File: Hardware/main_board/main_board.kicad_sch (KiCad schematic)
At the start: 115 parts, among them J1 ALARM, J2 RFID_CONN, J3 GPS_CONN, J4 USB_A, J5 DEBUG, J6 ANTENNA2, J7 Conn_01x04_Male, J8 BATT, SW1 SW_Push, SW2 SW_Push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

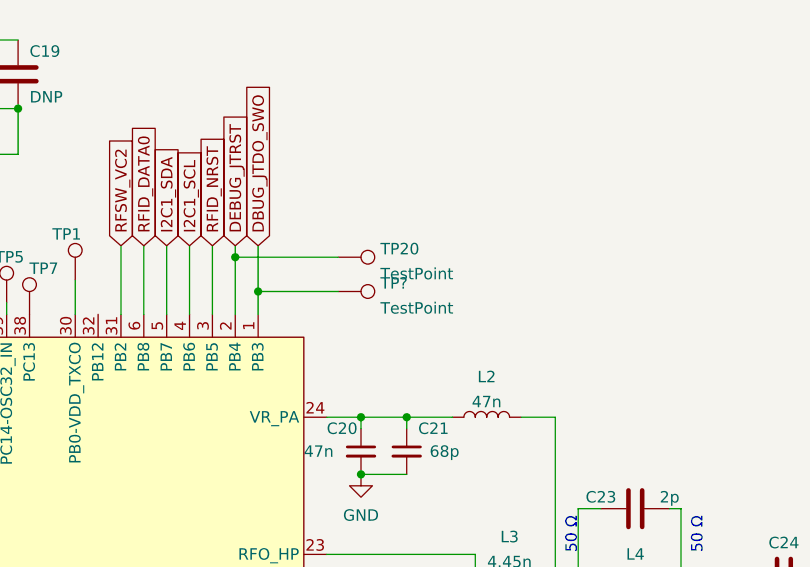
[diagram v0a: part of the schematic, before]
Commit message: all boards pass DRC and have appropriate silkscreens, will order tomorrow
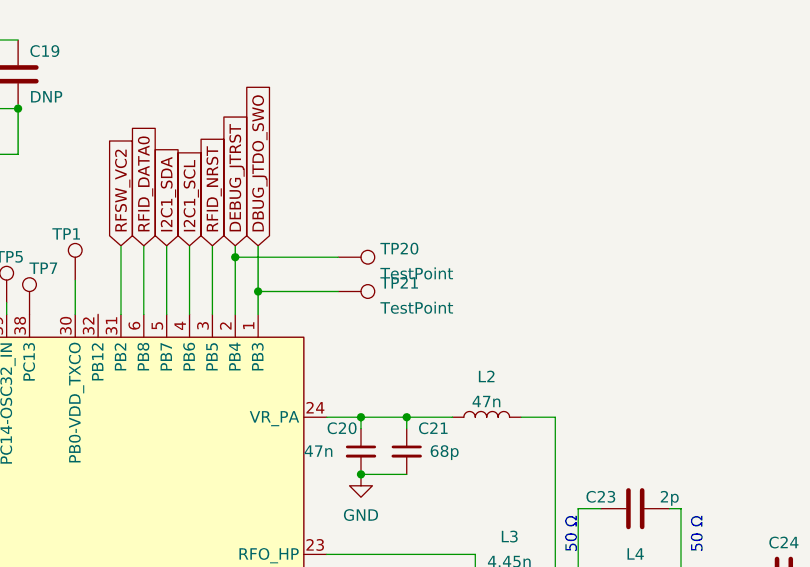
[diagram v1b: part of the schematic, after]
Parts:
- D5, D6, D7, D8: footprint LED_SMD:LED_0805_2012Metric -> LED_SMD:LED_0603_1608Metric
- H1, H2, H3, H4: footprint MountingHole:MountingHole_3.2mm_M3_Pad_Via -> MountingHole:MountingHole_2.2mm_M2_Pad_Via
- R15: footprint Resistor_SMD:R_0805_2012Metric_Pad1.20x1.40mm_HandSolder -> Resistor_SMD:R_0603_1608Metric
- TP21: renamed from TP?; footprint (none) -> TestPoint:TestPoint_Pad_1.0x1.0mm
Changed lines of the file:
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@@
       (effects (font (size 1.27 1.27)) (justify right))
     )
-    (property "Footprint" "LED_SMD:LED_0805_2012Metric" (id 2) (at 387.35 46.99 0)
+    (property "Footprint" "LED_SMD:LED_0603_1608Metric" (id 2) (at 387.35 46.99 0)
       (effects (font (size 1.27 1.27)) hide)
     )
@@
       (effects (font (size 1.27 1.27)) (justify left) hide)
     )
-    (property "Footprint" "MountingHole:MountingHole_3.2mm_M3_Pad_Via" (id 2) (at 161.29 176.53 0)
+    (property "Footprint" "MountingHole:MountingHole_2.2mm_M2_Pad_Via" (id 2) (at 161.29 176.53 0)
       (effects (font (size 1.27 1.27)) hide)
     )
@@
   (symbol (lib_id "Connector:TestPoint") (at 114.3 53.34 270) (unit 1)
     (in_bom yes) (on_board yes) (fields_autoplaced)
-    (property "Reference" "TP?" (id 0) (at 118.999 52.4315 90)
+    (property "Reference" "TP21" (id 0) (at 118.999 52.4315 90)
       (effects (font (size 1.27 1.27)) (justify left))
     )
@@
       (effects (font (size 1.27 1.27)) (justify left))
     )
-    (property "Footprint" "" (id 2) (at 114.3 58.42 0)
+    (property "Footprint" "TestPoint:TestPoint_Pad_1.0x1.0mm" (id 2) (at 114.3 58.42 0)
       (effects (font (size 1.27 1.27)) hide)
     )
@@
       (effects (font (size 1.27 1.27)) (justify left) hide)
     )
-    (property "Footprint" "MountingHole:MountingHole_3.2mm_M3_Pad_Via" (id 2) (at 187.96 176.53 0)
+    (property "Footprint" "MountingHole:MountingHole_2.2mm_M2_Pad_Via" (id 2) (at 187.96 176.53 0)
       (effects (font (size 1.27 1.27)) hide)
     )
@@
       (effects (font (size 1.27 1.27)) (justify right))
     )
-    (property "Footprint" "Resistor_SMD:R_0805_2012Metric_Pad1.20x1.40mm_HandSolder" (id 2) (at 387.35 40.64 0)
+    (property "Footprint" "Resistor_SMD:R_0603_1608Metric" (id 2) (at 387.35 40.64 0)
       (effects (font (size 1.27 1.27)) hide)
     )
@@
       (effects (font (size 1.27 1.27)) (justify right))
     )
-    (property "Footprint" "LED_SMD:LED_0805_2012Metric" (id 2) (at 365.76 170.18 0)
+    (property "Footprint" "LED_SMD:LED_0603_1608Metric" (id 2) (at 365.76 170.18 0)
       (effects (font (size 1.27 1.27)) hide)
     )
@@
       (effects (font (size 1.27 1.27)) (justify right))
     )
-    (property "Footprint" "LED_SMD:LED_0805_2012Metric" (id 2) (at 379.73 93.98 0)
+    (property "Footprint" "LED_SMD:LED_0603_1608Metric" (id 2) (at 379.73 93.98 0)
       (effects (font (size 1.27 1.27)) hide)
     )
@@
       (effects (font (size 1.27 1.27)) (justify right))
     )
-    (property "Footprint" "LED_SMD:LED_0805_2012Metric" (id 2) (at 374.65 215.9 0)
+    (property "Footprint" "LED_SMD:LED_0603_1608Metric" (id 2) (at 374.65 215.9 0)
       (effects (font (size 1.27 1.27)) hide)
     )
@@
       (effects (font (size 1.27 1.27)) (justify left) hide)
     )
-    (property "Footprint" "MountingHole:MountingHole_3.2mm_M3_Pad_Via" (id 2) (at 170.18 176.53 0)
+    (property "Footprint" "MountingHole:MountingHole_2.2mm_M2_Pad_Via" (id 2) (at 170.18 176.53 0)
       (effects (font (size 1.27 1.27)) hide)
     )
@@
       (effects (font (size 1.27 1.27)) (justify left) hide)
     )
-    (property "Footprint" "MountingHole:MountingHole_3.2mm_M3_Pad_Via" (id 2) (at 179.07 176.53 0)
+    (property "Footprint" "MountingHole:MountingHole_2.2mm_M2_Pad_Via" (id 2) (at 179.07 176.53 0)
       (effects (font (size 1.27 1.27)) hide)
     )
@@
     )
     (path "/90839a10-1748-447b-a8f6-5d8ba82ecd35"
-      (reference "D5") (unit 1) (value "LED") (footprint "LED_SMD:LED_0805_2012Metric")
+      (reference "D5") (unit 1) (value "LED") (footprint "LED_SMD:LED_0603_1608Metric")
     )
     (path "/b940411a-2d3b-4042-b778-3ae0cfa2823d"
-      (reference "D6") (unit 1) (value "LED") (footprint "LED_SMD:LED_0805_2012Metric")
+      (reference "D6") (unit 1) (value "LED") (footprint "LED_SMD:LED_0603_1608Metric")
     )
     (path "/940670f5-6e6c-448e-a873-e16d05c65f34"
-      (reference "D7") (unit 1) (value "LED") (footprint "LED_SMD:LED_0805_2012Metric")
+      (reference "D7") (unit 1) (value "LED") (footprint "LED_SMD:LED_0603_1608Metric")
     )
     (path "/16945da2-9bad-4b77-89c8-df5448d4ca01"
-      (reference "D8") (unit 1) (value "LED") (footprint "LED_SMD:LED_0805_2012Metric")
+      (reference "D8") (unit 1) (value "LED") (footprint "LED_SMD:LED_0603_1608Metric")
     )
     (path "/3430e4dd-38e6-4a37-ae77-90080133b97b"
@@
     )
     (path "/170fdaa5-055c-436c-b6f6-24ea6a52267d"
-      (reference "H1") (unit 1) (value "MountingHole_Pad") (footprint "MountingHole:MountingHole_3.2mm_M3_Pad_Via")
+      (reference "H1") (unit 1) (value "MountingHole_Pad") (footprint "MountingHole:MountingHole_2.2mm_M2_Pad_Via")
     )
     (path "/da2108a6-9ebf-4da0-9089-4dcd701dfe7b"
-      (reference "H2") (unit 1) (value "MountingHole_Pad") (footprint "MountingHole:MountingHole_3.2mm_M3_Pad_Via")
+      (reference "H2") (unit 1) (value "MountingHole_Pad") (footprint "MountingHole:MountingHole_2.2mm_M2_Pad_Via")
     )
     (path "/f8b8625a-b721-4616-992b-5ee8bcf0ac4c"
-      (reference "H3") (unit 1) (value "MountingHole_Pad") (footprint "MountingHole:MountingHole_3.2mm_M3_Pad_Via")
+      (reference "H3") (unit 1) (value "MountingHole_Pad") (footprint "MountingHole:MountingHole_2.2mm_M2_Pad_Via")
     )
     (path "/33b7367b-d0fe-4560-9ed0-8a16c0f28c10"
-      (reference "H4") (unit 1) (value "MountingHole_Pad") (footprint "MountingHole:MountingHole_3.2mm_M3_Pad_Via")
+      (reference "H4") (unit 1) (value "MountingHole_Pad") (footprint "MountingHole:MountingHole_2.2mm_M2_Pad_Via")
     )
     (path "/e78b33e4-67a7-4a78-82b4-0a90c03cdc93"
@@
     )
     (path "/744e1123-f449-4e63-bfb9-752077622150"
-      (reference "R15") (unit 1) (value "200R") (footprint "Resistor_SMD:R_0805_2012Metric_Pad1.20x1.40mm_HandSolder")
+      (reference "R15") (unit 1) (value "200R") (footprint "Resistor_SMD:R_0603_1608Metric")
     )
     (path "/9b4844fe-2f67-43fb-8971-7a90772379d4"
@@
     )
     (path "/1e5e8b9b-9231-4794-a36d-b2f8996eb04d"
-      (reference "TP?") (unit 1) (value "TestPoint") (footprint "")
+      (reference "TP21") (unit 1) (value "TestPoint") (footprint "TestPoint:TestPoint_Pad_1.0x1.0mm")
     )
     (path "/e3760479-0a57-413a-a85d-581fad0f8c75"
